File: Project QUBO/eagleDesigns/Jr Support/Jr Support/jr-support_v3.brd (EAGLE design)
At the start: 203.2 x 127 mm, 197 parts, among them U1 PCA9685

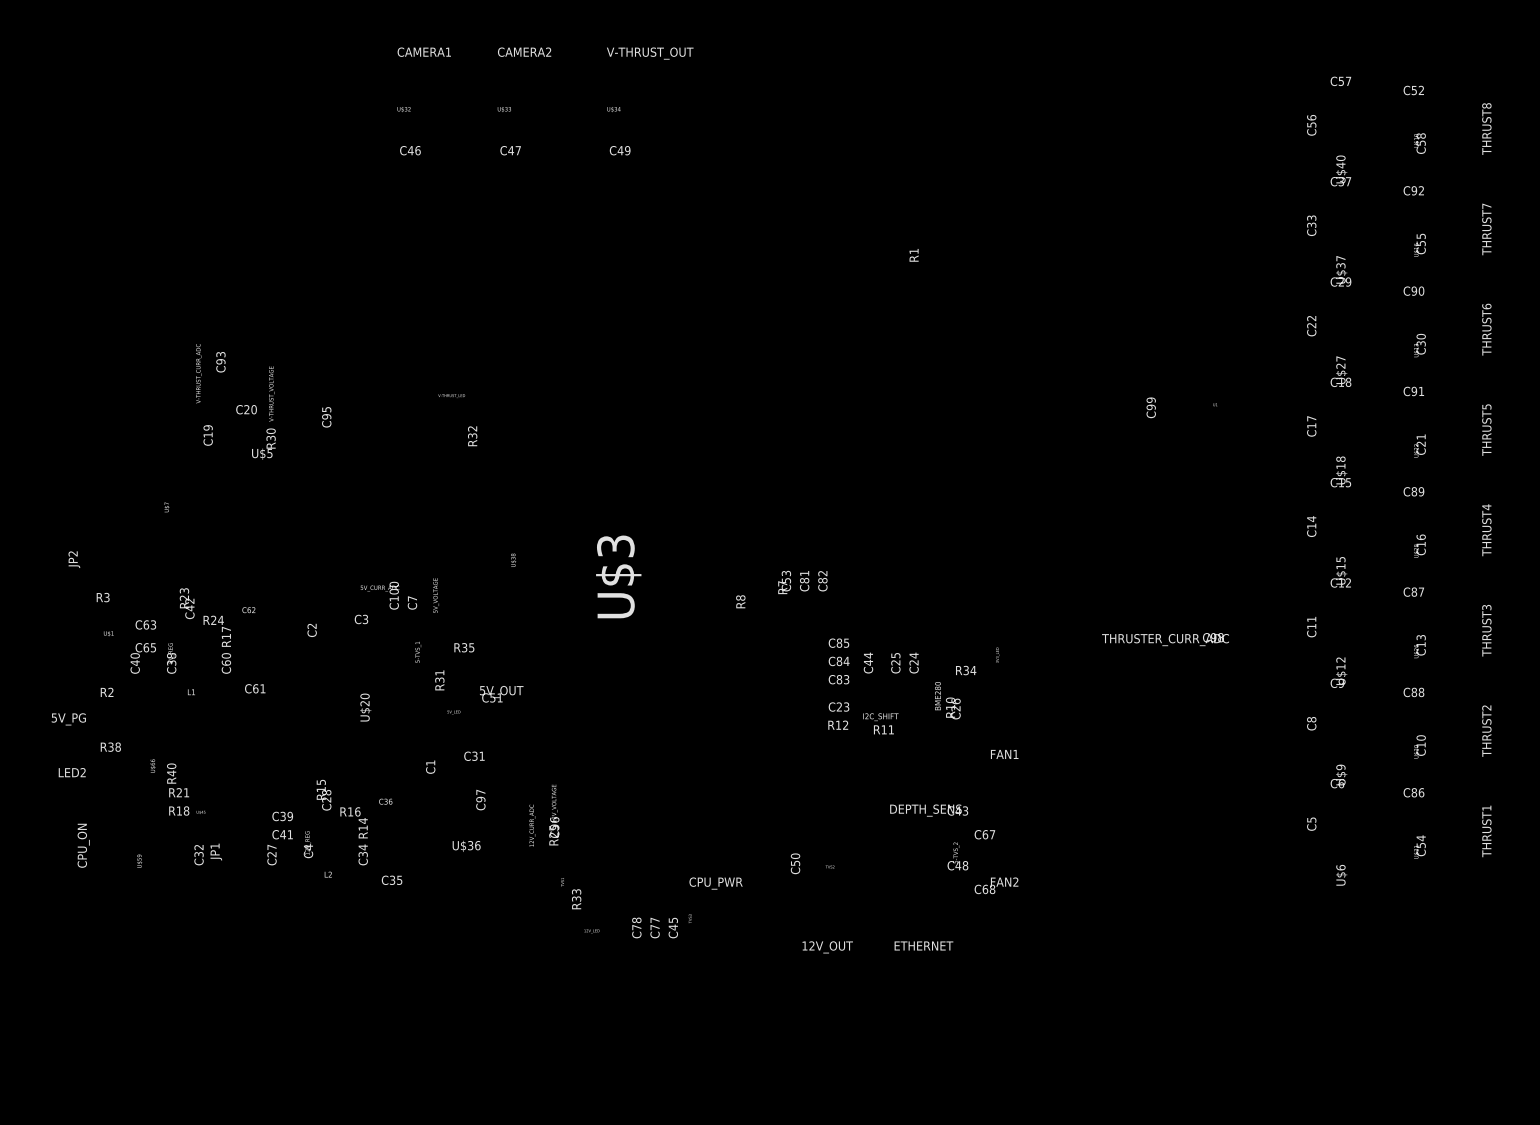
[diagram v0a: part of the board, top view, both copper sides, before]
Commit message: 
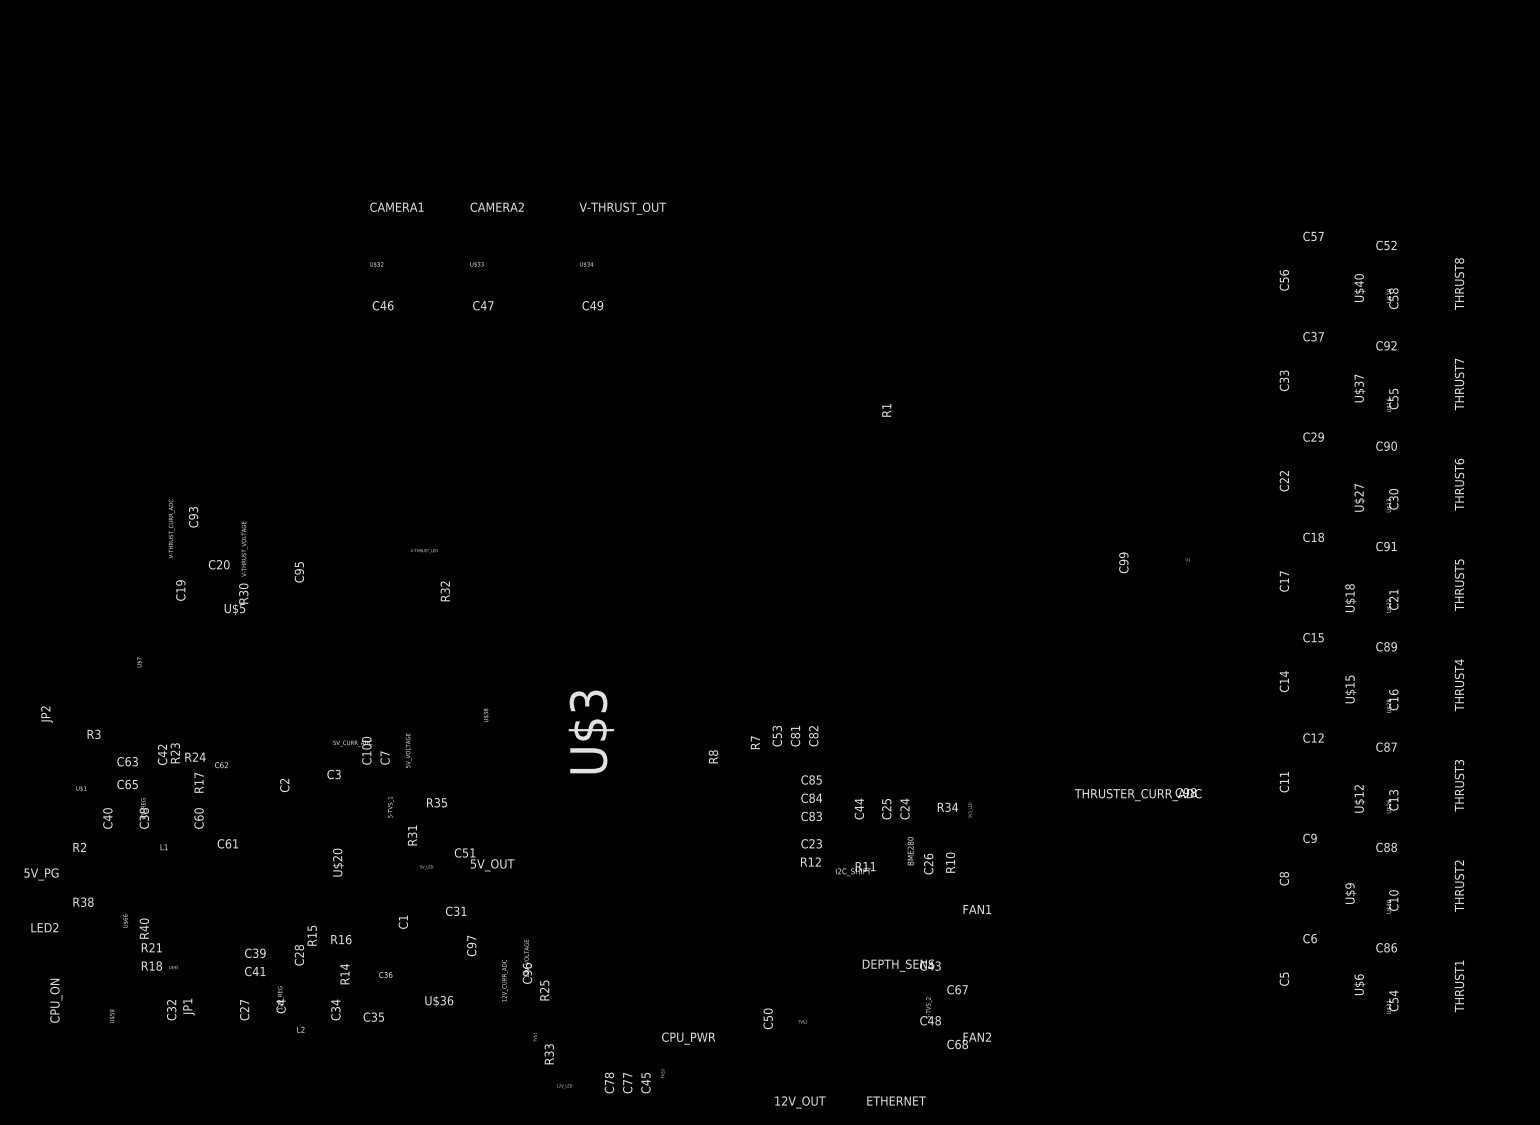
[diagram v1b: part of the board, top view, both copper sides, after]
